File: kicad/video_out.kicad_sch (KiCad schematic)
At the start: 39 parts, among them J6 3.5 mm, J7 VGA, U16 ATF22V10C-10PU, U22 SN74F377AN, U23 SN74F377AN, U36 SN74HCT574N

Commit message: Main board layout: 290 x 140 mm outline, dimensions, connectors and slots placed
gen_kicad_pcb.py places the outline, dimensions, mounting holes, back-edge
I/O (USB-C, audio, VGA, PS/2), left-side SW1/SW2/SD, right-side SNES ports,
cartridge slot J8, expansion slots J9-J12 and keyboard header J1, linked to
the schematic symbols, and draws docs/placard_board_layout.png.
gen_kicad_connectors.py writes preliminary footprints for the parts KiCad
has none for; the schematic generator now assigns all connector footprints.

Co-Authored-By: Claude Opus 5.5 (1M context) <noreply@anthropic.com>
Claude-Session: https://claude.ai/code/session_013qXQudFqhMaBbYKyavQCXN
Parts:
- J6: footprint (none) -> Connector_Audio:Jack_3.5mm_CUI_SJ1-3523N_Horizontal
- J7: footprint (none) -> Connector_Dsub:DSUB-15-HD_Female_Horizontal_P2.29x1.98mm_EdgePinOffset3.03mm_Housed_MountingHolesOffset4.94mm
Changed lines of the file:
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@@
   (wire (pts (xy 306.07 109.22) (xy 306.07 111.76)) (stroke (width 0) (type default)))
   (symbol (lib_id "power:GND") (at 306.07 111.76 270) (unit 1) (in_bom yes) (on_board yes) (dnp no) (property "Reference" "#PWR0917" (at 306.07 111.76 0) (effects (font (size 1.27 1.27)) hide)) (property "Value" "GND" (at 297.72 111.76 90) (effects (font (size 2 2)) hide)) (property "Footprint" "" (at 306.07 111.76 0) (effects (font (size 1.27 1.27)) hide)) (property "Datasheet" "" (at 306.07 111.76 0) (effects (font (size 1.27 1.27)) hide)) (pin "1") (instances (project "placard" (path "/e3450542-4ffc-59d4-a4a7-45636233928a/53445658-004f-5a3f-8e51-bf0246e5367e" (reference "#PWR0917") (unit 1)))))
-  (symbol (lib_id "placard_std:DE15_Receptacle_HighDensity_MountingHoles") (at 316.23 101.6 0) (unit 1) (in_bom yes) (on_board yes) (dnp no) (property "Reference" "J7" (at 311 84 0) (effects (font (size 2.54 2.54) bold) (justify left bottom))) (property "Value" "VGA" (at 311 126 0) (effects (font (size 2 2)) (justify left top))) (property "Footprint" "" (at 316.23 101.6 0) (effects (font (size 1.27 1.27)) hide)) (property "Datasheet" " ~" (at 316.23 101.6 0) (effects (font (size 1.27 1.27)) hide)) (property "Manufacturer" "" (at 316.23 101.6 0) (effects (font (size 1.27 1.27)) hide)) (property "MPN" "" (at 316.23 101.6 0) (effects (font (size 1.27 1.27)) hide)) (pin "0") (pin "1") (pin "10") (pin "11") (pin "12") (pin "13") (pin "14") (pin "15") (pin "2") (pin "3") (pin "4") (pin "5") (pin "6") (pin "7") (pin "8") (pin "9") (instances (project "placard" (path "/e3450542-4ffc-59d4-a4a7-45636233928a/53445658-004f-5a3f-8e51-bf0246e5367e" (reference "J7") (unit 1)))))
+  (symbol (lib_id "placard_std:DE15_Receptacle_HighDensity_MountingHoles") (at 316.23 101.6 0) (unit 1) (in_bom yes) (on_board yes) (dnp no) (property "Reference" "J7" (at 311 84 0) (effects (font (size 2.54 2.54) bold) (justify left bottom))) (property "Value" "VGA" (at 311 126 0) (effects (font (size 2 2)) (justify left top))) (property "Footprint" "Connector_Dsub:DSUB-15-HD_Female_Horizontal_P2.29x1.98mm_EdgePinOffset3.03mm_Housed_MountingHolesOffset4.94mm" (at 316.23 101.6 0) (effects (font (size 1.27 1.27)) hide)) (property "Datasheet" " ~" (at 316.23 101.6 0) (effects (font (size 1.27 1.27)) hide)) (property "Manufacturer" "" (at 316.23 101.6 0) (effects (font (size 1.27 1.27)) hide)) (property "MPN" "" (at 316.23 101.6 0) (effects (font (size 1.27 1.27)) hide)) (pin "0") (pin "1") (pin "10") (pin "11") (pin "12") (pin "13") (pin "14") (pin "15") (pin "2") (pin "3") (pin "4") (pin "5") (pin "6") (pin "7") (pin "8") (pin "9") (instances (project "placard" (path "/e3450542-4ffc-59d4-a4a7-45636233928a/53445658-004f-5a3f-8e51-bf0246e5367e" (reference "J7") (unit 1)))))
   (wire (pts (xy 248.92 88.9) (xy 264.16 88.9)) (stroke (width 0) (type default)))
   (wire (pts (xy 248.92 93.98) (xy 264.16 93.98)) (stroke (width 0) (type default)))
@@
   (wire (pts (xy 276.86 243.84) (xy 274.32 243.84)) (stroke (width 0) (type default)))
   (symbol (lib_id "power:GNDA") (at 274.32 243.84 270) (unit 1) (in_bom yes) (on_board yes) (dnp no) (property "Reference" "#PWR0927" (at 274.32 243.84 0) (effects (font (size 1.27 1.27)) hide)) (property "Value" "GNDA" (at 265.02 243.84 90) (effects (font (size 2 2)) hide)) (property "Footprint" "" (at 274.32 243.84 0) (effects (font (size 1.27 1.27)) hide)) (property "Datasheet" "" (at 274.32 243.84 0) (effects (font (size 1.27 1.27)) hide)) (pin "1") (instances (project "placard" (path "/e3450542-4ffc-59d4-a4a7-45636233928a/53445658-004f-5a3f-8e51-bf0246e5367e" (reference "#PWR0927") (unit 1)))))
-  (symbol (lib_id "placard_std:AudioJack3") (at 281.94 241.3 180) (unit 1) (in_bom yes) (on_board yes) (dnp no) (property "Reference" "J6" (at 278 232.26 0) (effects (font (size 2.54 2.54) bold) (justify right top))) (property "Value" "3.5 mm" (at 285 246.76 0) (effects (font (size 2 2)) (justify right bottom))) (property "Footprint" "" (at 281.94 241.3 0) (effects (font (size 1.27 1.27)) hide)) (property "Datasheet" "~" (at 281.94 241.3 0) (effects (font (size 1.27 1.27)) hide)) (property "Manufacturer" "" (at 281.94 241.3 0) (effects (font (size 1.27 1.27)) hide)) (property "MPN" "" (at 281.94 241.3 0) (effects (font (size 1.27 1.27)) hide)) (pin "R") (pin "S") (pin "T") (instances (project "placard" (path "/e3450542-4ffc-59d4-a4a7-45636233928a/53445658-004f-5a3f-8e51-bf0246e5367e" (reference "J6") (unit 1)))))
+  (symbol (lib_id "placard_std:AudioJack3") (at 281.94 241.3 180) (unit 1) (in_bom yes) (on_board yes) (dnp no) (property "Reference" "J6" (at 278 232.26 0) (effects (font (size 2.54 2.54) bold) (justify right top))) (property "Value" "3.5 mm" (at 285 246.76 0) (effects (font (size 2 2)) (justify right bottom))) (property "Footprint" "Connector_Audio:Jack_3.5mm_CUI_SJ1-3523N_Horizontal" (at 281.94 241.3 0) (effects (font (size 1.27 1.27)) hide)) (property "Datasheet" "~" (at 281.94 241.3 0) (effects (font (size 1.27 1.27)) hide)) (property "Manufacturer" "" (at 281.94 241.3 0) (effects (font (size 1.27 1.27)) hide)) (property "MPN" "" (at 281.94 241.3 0) (effects (font (size 1.27 1.27)) hide)) (pin "R") (pin "S") (pin "T") (instances (project "placard" (path "/e3450542-4ffc-59d4-a4a7-45636233928a/53445658-004f-5a3f-8e51-bf0246e5367e" (reference "J6") (unit 1)))))
   (wire (pts (xy 242.57 238.76) (xy 256.54 238.76)) (stroke (width 0) (type default)))
   (wire (pts (xy 256.54 238.76) (xy 274.32 238.76)) (stroke (width 0) (type default)))

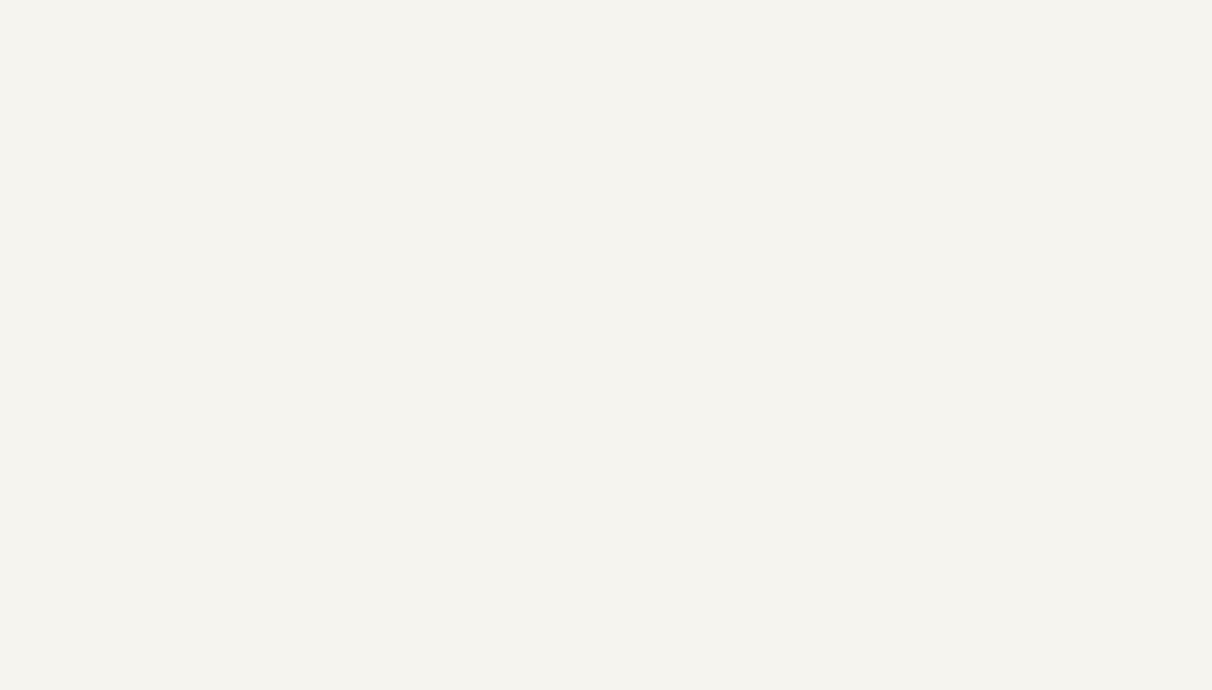
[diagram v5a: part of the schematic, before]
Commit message: Through-hole ESD clamps on external I/O; D7 TVS to through-hole SA5.0A
BAT85 steering pairs to +5V and GND on every PS/2 and SNES signal line
(D8-D21, shared port sheet) and on the VGA syncs (D22-D25, video sheet).
D7 changes from the SMD SMAJ5.0A to the DO-15 SA5.0A (through hole
wherever possible). BOM, docs and PDFs regenerated.

Co-Authored-By: Claude Opus 5.5 (1M context) <noreply@anthropic.com>
Claude-Session: https://claude.ai/code/session_01L9AkLuEg13EebxDmgXsaEp
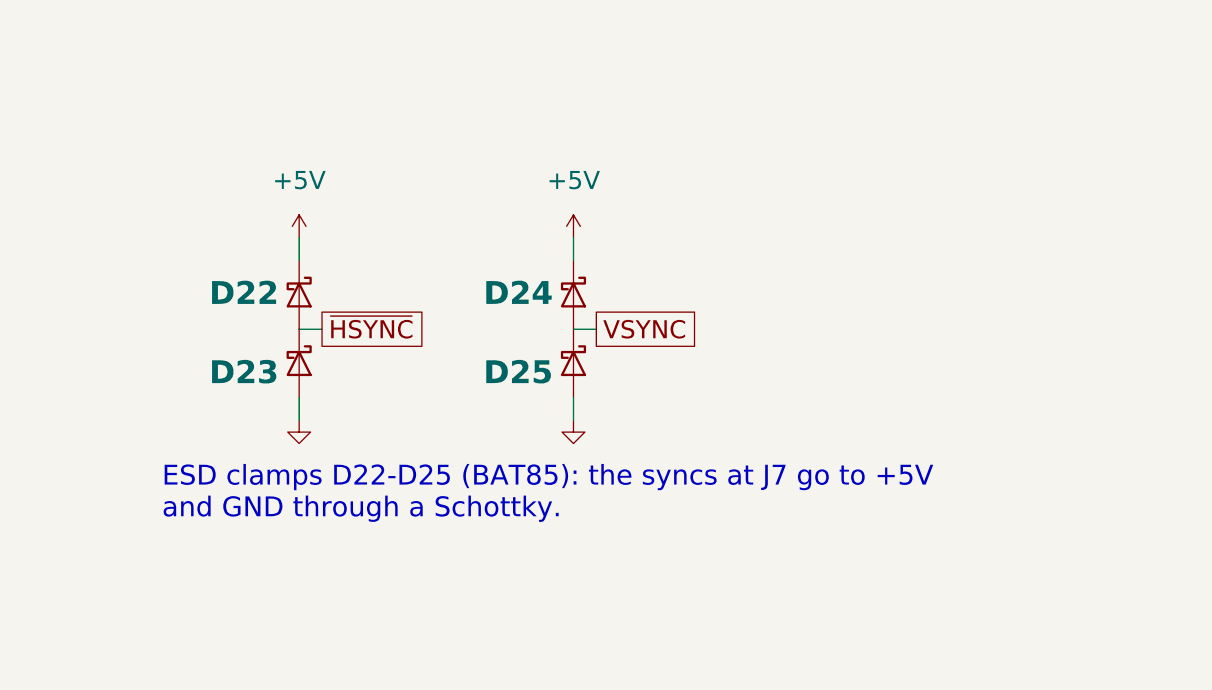
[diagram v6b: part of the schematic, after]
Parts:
- added D22, D23, D24, D25: BAT85, Diode_THT:D_DO-35_SOD27_P7.62mm_Horizontal, symbol placard_std:D_Schottky
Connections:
- net +5V: now also D22.1 (K), D24.1 (K)
- net GND: now also D23.2 (A), D25.2 (A)
- net VSYNC: now also D24.2 (A), D25.1 (K)
- net ~{HSYNC}: now also D22.2 (A), D23.1 (K)
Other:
- note added: "ESD clamps D22-D25 (BAT85): the syncs at J7 go to +5V"
- note added: "and GND through a Schottky."

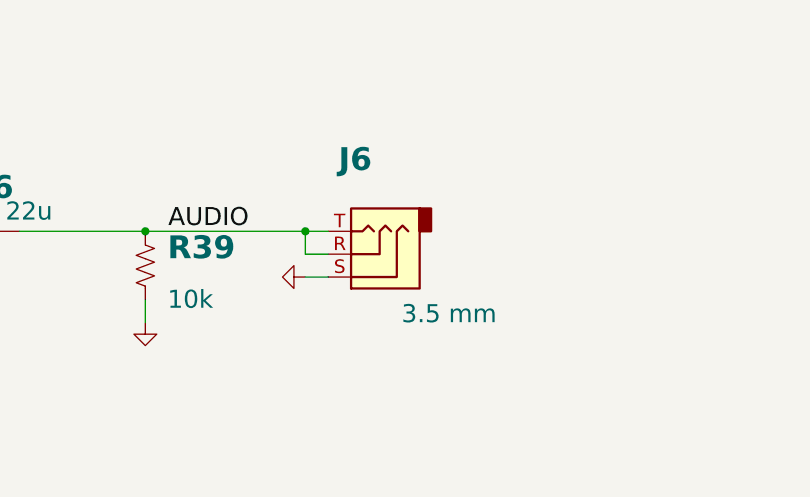
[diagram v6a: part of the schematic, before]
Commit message: Part numbers for the remaining parts; J6 Tensility 54-00174; optional J1 and J9-J12
Every schematic part gets Manufacturer/MPN: Yageo MFR-25 resistors by value,
Bourns 4609X networks, KEMET/TDK ceramics, Panasonic FR electrolytics, ECS
oscillator, Assmann VGA, Sullins headers, Wurth box header, Cherry switches.
Sockets get On Shore numbers (0.3" 24/28-pin are ED241DT/ED281DT; ED28DT is
0.6"). J6 becomes the Tensility 54-00174 TRRS jack with a footprint drawn
from its datasheet. Digi-Key prices from Justin for the oscillator, VGA and
audio jack. The expansion slot sockets and the keyboard header are optional,
with a BOM total without them.

Co-Authored-By: Claude Opus 5.5 (1M context) <noreply@anthropic.com>
Claude-Session: https://claude.ai/code/session_01L9AkLuEg13EebxDmgXsaEp
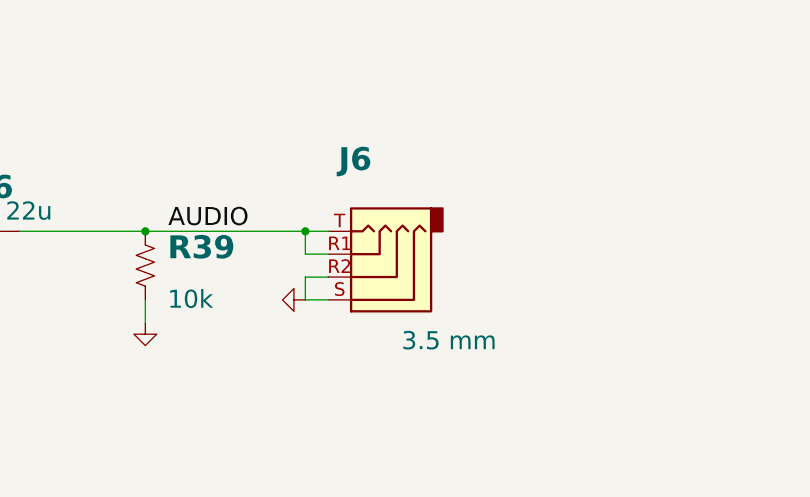
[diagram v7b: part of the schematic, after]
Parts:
- removed J6: 3.5 mm, Connector_Audio:Jack_3.5mm_CUI_SJ1-3523N_Horizontal, symbol placard_std:AudioJack3
- added J6: 3.5 mm, placard:Jack_3.5mm_Tensility_54-00174_Horizontal, symbol placard_std:AudioJack4
- C16, C22, C23, C36: MPN (none) -> C320C104K5R5TA; Manufacturer (none) -> KEMET
- C44: MPN (none) -> EEU-FR1C221; Manufacturer (none) -> Panasonic
- C45: MPN (none) -> C320C153K1G5TA; Manufacturer (none) -> KEMET
- C46: MPN (none) -> FG24X5R1A226MRT06; Manufacturer (none) -> TDK
- J7: MPN (none) -> A-HDF 15 A-KG/T; Manufacturer (none) -> Assmann WSW
- R14, R17: MPN (none) -> MFR-25FBF52-3K24; Manufacturer (none) -> Yageo
- R15, R18: MPN (none) -> MFR-25FBF52-1K69; Manufacturer (none) -> Yageo
- R16, R19: MPN (none) -> MFR-25FBF52-825R; Manufacturer (none) -> Yageo
- R20: MPN (none) -> MFR-25FBF52-1K43; Manufacturer (none) -> Yageo
- R21: MPN (none) -> MFR-25FBF52-715R; Manufacturer (none) -> Yageo
- R22: MPN (none) -> MFR-25FBF52-2R2; Manufacturer (none) -> Yageo
- R23, R24, R25, R26, R27, R28, R29, R30, R31: MPN (none) -> MFR-25FBF52-2K; Manufacturer (none) -> Yageo
- R32, R33, R34, R35, R36, R37, R38: MPN (none) -> MFR-25FBF52-1K; Manufacturer (none) -> Yageo
- R39: MPN (none) -> MFR-25FBF52-10K; Manufacturer (none) -> Yageo
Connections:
- net AUDIO: now also J6.R1, J6.T
- net GNDA: now also J6.R2, J6.S

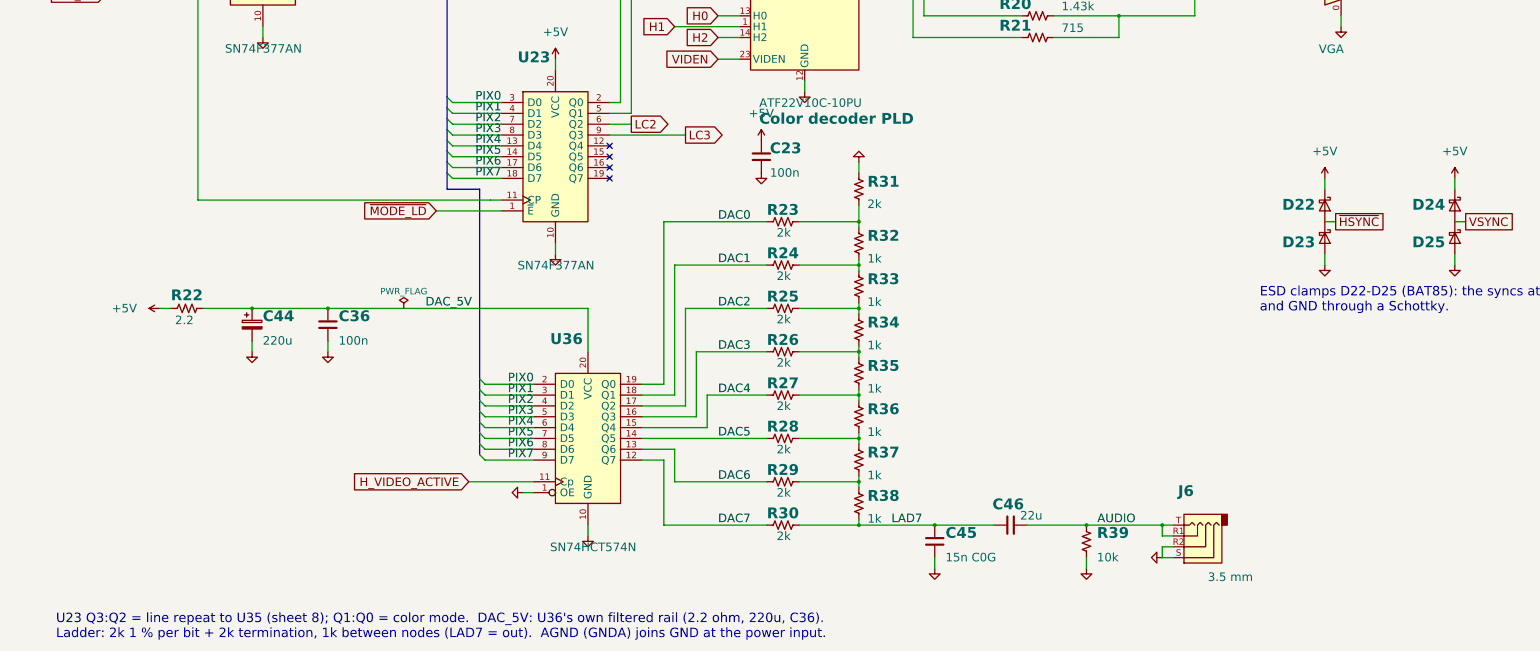
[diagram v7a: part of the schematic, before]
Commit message: Schematic: row tint and blank line
Video out sheet: U23 is a 74HCT377; Q6:Q4 drive the row tint (R56-R58
910 ohm, two 1N4148 per channel into VGA_R/G/B, BAT85 D27-D29 from each
node to VIDEN).  Video timing sheet: U23 Q7 (LC7) to H counter pin 6.
New Device:D symbol in placard_std; H counter symbol has LC7.  The
regenerated symbol library also brings the memory control /WE pin type
up to date.  BOM not regenerated yet.

Co-Authored-By: Claude Opus 5.5 (1M context) <noreply@anthropic.com>
Claude-Session: https://claude.ai/code/session_01AyS52y3xy4qvxwvt915gG3
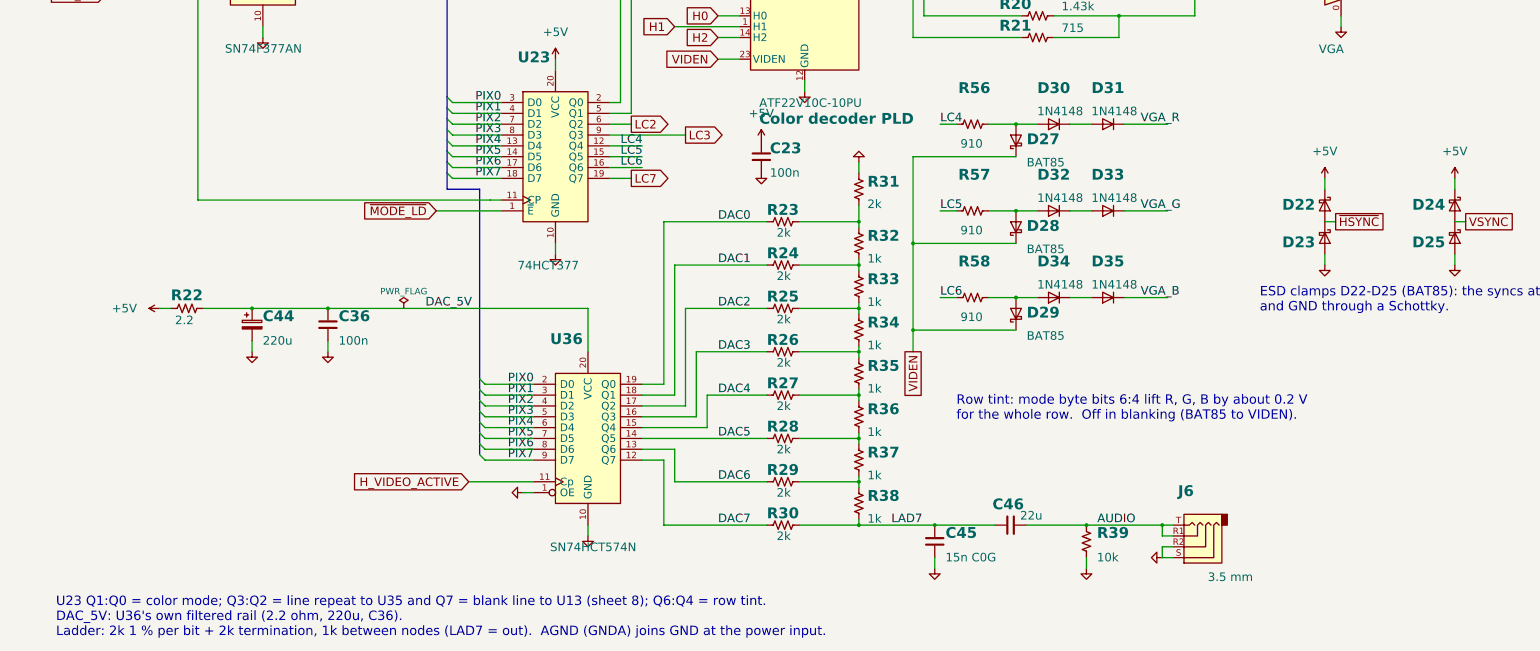
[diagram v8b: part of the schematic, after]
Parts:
- added D27, D28, D29: BAT85, Diode_THT:D_DO-35_SOD27_P7.62mm_Horizontal, symbol placard_std:D_Schottky
- added D30, D31, D32, D33, D34, D35: 1N4148, Diode_THT:D_DO-35_SOD27_P7.62mm_Horizontal, symbol placard_std:D
- added R56, R57, R58: 910, Resistor_THT:R_Axial_DIN0207_L6.3mm_D2.5mm_P10.16mm_Horizontal, symbol placard_std:R_US
- U23: value SN74F377AN -> 74HCT377; MPN SN74F377AN -> (none); Manufacturer Texas Instruments -> (none)
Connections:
- net VGA_B: now also D35.1 (K)
- net VGA_G: now also D33.1 (K)
- net VGA_R: now also D31.1 (K)
- net VIDEN: now also D27.1 (K), D28.1 (K), D29.1 (K)
- net LC4: now reaches U23.12 (Q4)
- net LC4: now also R56.1
- net LC5: now reaches U23.15 (Q5)
- net LC5: now also R57.1
- net LC6: now reaches U23.16 (Q6)
- net LC6: now also R58.1
- net LC7: now reaches U23.19 (Q7)
- new net: D27.2 (A), D30.2 (A), R56.2
- new net: D30.1 (K), D31.2 (A)
- new net: D34.1 (K), D35.2 (A)
- new net: D29.2 (A), D34.2 (A), R58.2
- new net: D32.1 (K), D33.2 (A)
- new net: D28.2 (A), D32.2 (A), R57.2
- no-connect marks 9 -> 5
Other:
- note added: "DAC_5V: U36's own filtered rail (2.2 ohm, 220u, C36)."
- note added: "Row tint: mode byte bits 6:4 lift R, G, B by about 0.2 V"
- note added: "U23 Q1:Q0 = color mode; Q3:Q2 = line repeat to U35 and Q7 = blank line to U13 (sheet 8); Q6:Q4 = row tint."
- note added: "for the whole row. Off in blanking (BAT85 to VIDEN)."
- note removed: "U23 Q3:Q2 = line repeat to U35 (sheet 8); Q1:Q0 = color mode. DAC_5V: U36's own filtered rail (2.2 ohm, 220u, C36)."
